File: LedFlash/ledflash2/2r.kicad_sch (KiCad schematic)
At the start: 3 parts

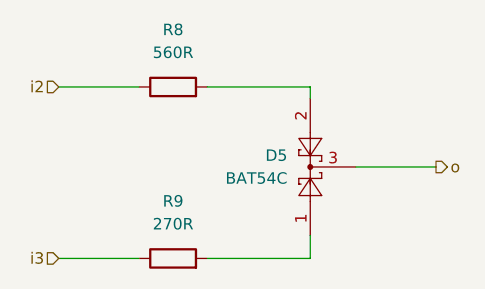
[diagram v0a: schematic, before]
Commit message: Update LedFlash (capacitors footprints and LED symbol)
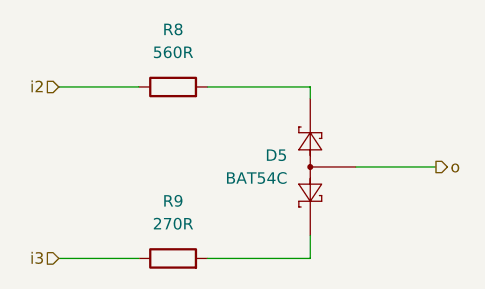
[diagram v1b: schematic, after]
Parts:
- D5: symbol Diode:BAT54C -> Diode:BAT54A
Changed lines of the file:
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@@
 	)
 	(symbol
-		(lib_id "Diode:BAT54C")
+		(lib_id "Diode:BAT54A")
 		(at 165.1 113.03 90)
 		(unit 1)

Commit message: Updated Value BAT54C to BAT54A
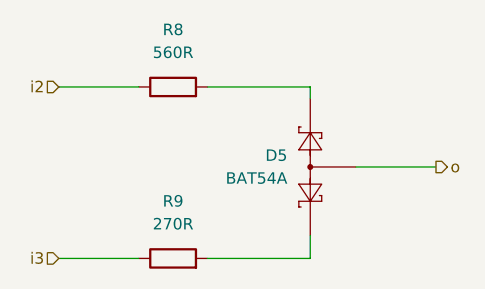
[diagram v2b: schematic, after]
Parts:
- D5: value BAT54C -> BAT54A
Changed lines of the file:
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@@
 			)
 		)
-		(property "Value" "BAT54C"
+		(property "Value" "BAT54A"
 			(at 162.56 114.2999 90)
 			(effects
